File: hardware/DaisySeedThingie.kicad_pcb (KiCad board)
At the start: 2 copper layers, 236.2 x 124.5 mm, 66 parts, among them J1 LEDS, J10 AUDIO IN LR, J11 AUDIO IN L, J12 AUDIO IN R, J13 AUDIO OUT LR, J14 AUDIO OUT L, J15 AUDIO OUT R, J16 MIDI IN, J17 MIDI OUT, J18 MIDI IN, J19 MIDI OUT, J2 DC IN, J20 A, J21 B, J22 C, J23 D, J3 DAISY PINS, J4 COMPONENTS, J5 DAISY PINS, J6 Yamaichi PJS008-4100-0-VE, J7 MICRO SD, J8 AUDIO IN, J9 AUDIO OUT, SW1 ENCODER, SW2 A, SW3 C, SW4 B, SW5 D, U1 DAISY SEED, U2 H11L1, U3 128x64

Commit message: Restructure
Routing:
- net +3.3V: track 390.1 -> 0.00 mm, vias 1 -> 0
- net D0: track 352.6 -> 0.00 mm, vias 3 -> 0
- net D27: track 347.4 -> 0.00 mm, vias 2 -> 0
- net AUDIO_OUT_L: track 345.4 -> 0.00 mm, vias 4 -> 0
- net +VIN: track 337.7 -> 0.00 mm, vias 3 -> 0
- net D3: track 336.2 -> 0.00 mm, vias 3 -> 0
- net D9: track 331.9 -> 0.00 mm, vias 1 -> 0
- net AUDIO_IN_R: track 326.7 -> 0.00 mm, vias 3 -> 0
- net AUDIO_IN_L: track 322.2 -> 0.00 mm, vias 3 -> 0
- net AUDIO_OUT_R: track 310.4 -> 0.00 mm, vias 1 -> 0
- net D12: track 309.3 -> 0.00 mm, vias 3 -> 0
- net D10: track 303.1 -> 0.00 mm, vias 2 -> 0
- net D1: track 300.4 -> 0.00 mm, vias 3 -> 0
- net D11: track 295.0 -> 0.00 mm, vias 3 -> 0
- net D22: track 294.7 -> 0.00 mm, vias 4 -> 0
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
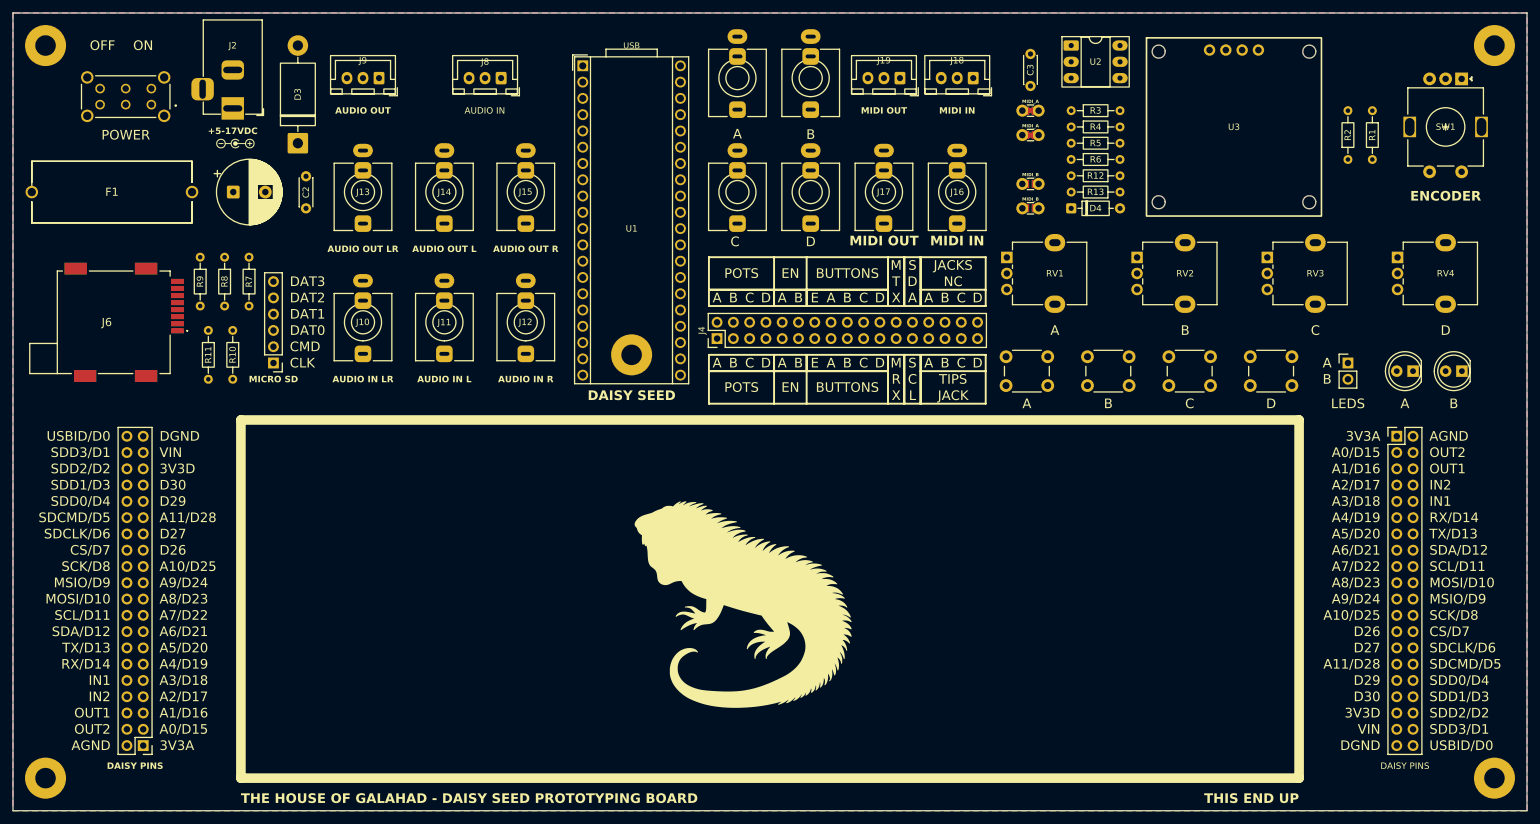
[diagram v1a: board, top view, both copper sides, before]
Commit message: Restore after bad merge
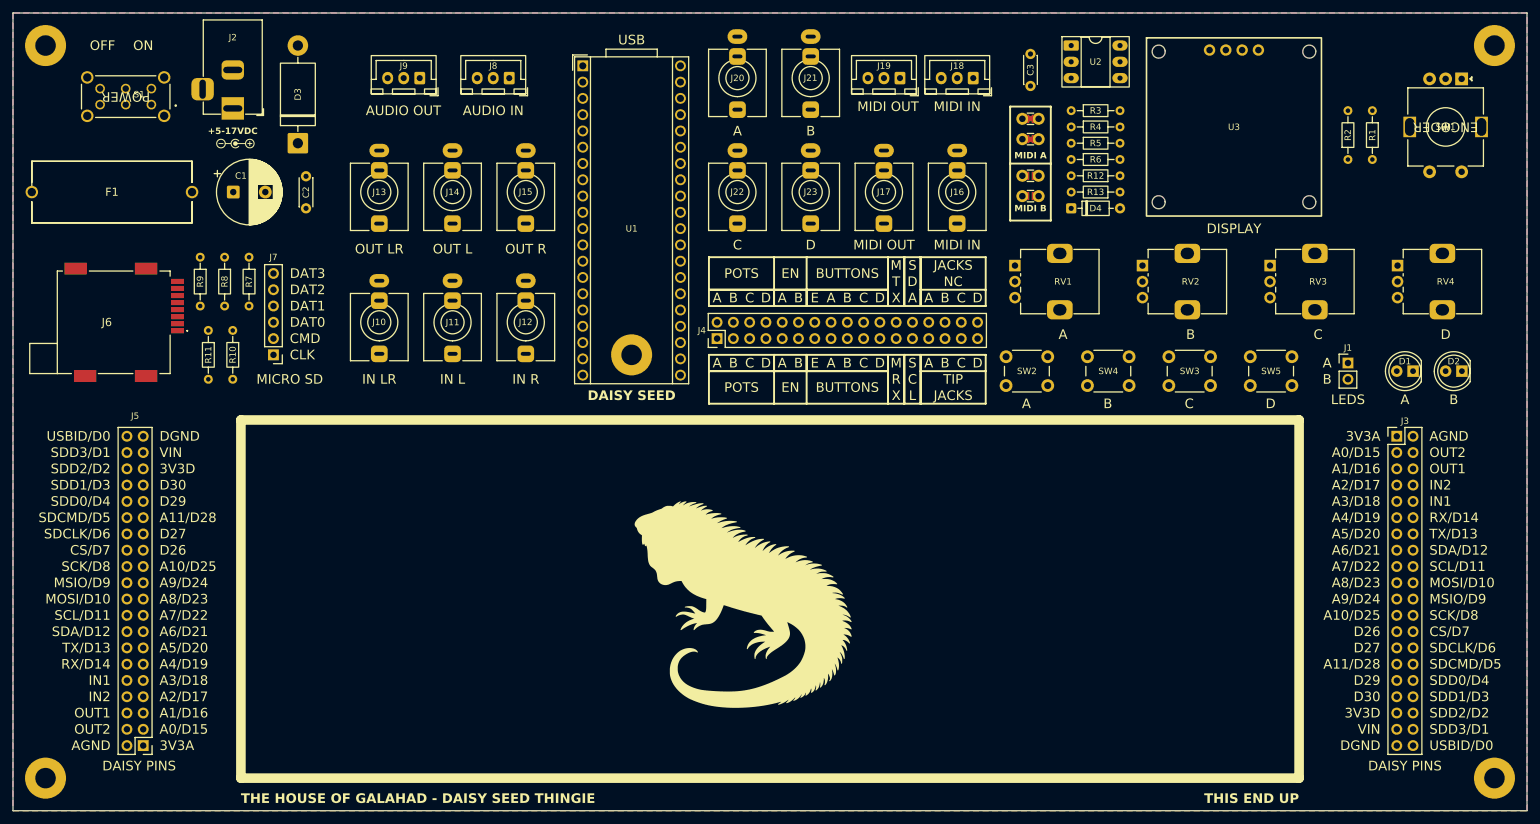
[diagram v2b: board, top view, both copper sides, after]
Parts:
- D1: value A -> RED
- D2: value B -> RED
- F1: value Fuse -> 5x20mm
- J1: value LEDS -> 01x02 PIN CONNECTOR
- J10: value AUDIO IN LR -> STEREO 3.5mm
- J11: value AUDIO IN L -> MONO 3.5mm
- J12: value AUDIO IN R -> MONO 3.5mm
- J13: value AUDIO OUT LR -> STEREO 3.5mm
- J14: value AUDIO OUT L -> MONO 3.5mm
- J15: value AUDIO OUT R -> MONO 3.5mm
- J16: value MIDI IN -> STEREO 3.5mm
- J17: value MIDI OUT -> STEREO 3.5mm
- J18: value MIDI IN -> JST 01x03
- J19: value MIDI OUT -> JST 01x03
- J2: value DC IN -> DC Barrel Jack
- J20: value A -> MONO 3.5mm
- J21: value B -> MONO 3.5mm
- J22: value C -> MONO 3.5mm
- J23: value D -> MONO 3.5mm
- J3, J5: value DAISY PINS -> 02x20 PIN CONNECTOR
- J4: value COMPONENTS -> 02x17 PIN CONNECTOR
- J7: value MICRO SD -> 01x06 PIN CONNECTOR
- J8: value AUDIO IN -> JST 01x03
- J9: value AUDIO OUT -> JST 01x03
- JP1, JP4: value MIDI_B -> JUMPER
- JP2, JP3: value MIDI_A -> JUMPER
- RV1, RV2, RV3, RV4: footprint Desval:Potentiometer_Alpha_RD901F-40-00D_Single_Vertical -> Desval:Potentiometer_Alps_RK09K_Single_Vertical
- S1: value POWER -> EG2219
- SW1: value ENCODER -> EN11C
- SW2: value A -> SW_PUSH_6mm
- SW3: value C -> SW_PUSH_6mm
- SW4: value B -> SW_PUSH_6mm
- SW5: value D -> SW_PUSH_6mm
- U3: value 128x64 -> SSD1306 0.96" OLED I2C
- moved J9 6.35 mm to (81.2, 53.3)
- moved J10 2.54 mm to (74.9, 91.4)
- moved J13 2.54 mm to (74.9, 71.1)
- moved JP4 1.91 mm to (176.5, 71.8), turned to 0 degrees
- moved RV1 1.80 mm to (181.6, 85.1), turned to 0 degrees
- moved RV2 1.53 mm to (201.5, 85.1), turned to 0 degrees
- moved RV3 1.34 mm to (221.4, 85.1), turned to 0 degrees
- moved J7 1.27 mm to (58.4, 96.5)
- moved RV4 1.27 mm to (241.3, 85.1), turned to 0 degrees
- moved J11 1.27 mm to (86.4, 91.4)
- moved J14 1.27 mm to (86.4, 71.1)
- moved J8 1.27 mm to (95.2, 53.3)
- moved JP1 1.27 mm to (176.5, 68.6), turned to 0 degrees
- moved JP2 1.27 mm to (176.5, 59.7), turned to 0 degrees
- moved JP3 0.64 mm to (176.5, 62.9), turned to 0 degrees
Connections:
- S1 pad S1: Net-(J2-Pad2) -> GND
- S1 pad S2: Net-(J2-Pad2) -> GND
- S1 pad S3: Net-(J2-Pad2) -> GND
- S1 pad S4: Net-(J2-Pad2) -> GND
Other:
- board text added: "${COMPANY} - ${TITLE}"
- board text added: "EMAIL: ${EMAIL} GITHUB: ${GITHUB}"
- board text added: "REV ${REVISION} - ${ISSUE_DATE}"
- board text added: "TIP"
- board text removed: "JACK"
- board text removed: "REV B - 2026-04-05 paul.f.burdette@gmail.com"
- board text removed: "THE HOUSE OF GALAHAD - DAISY SEED PROTOTYPING BOARD"
- board text removed: "TIPS"

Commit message: Initial Revision B
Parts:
- removed H5: MountingHole_Pad, MountingHole:MountingHole_3.2mm_M3_Pad
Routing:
- net GND: track 0.00 -> 883.1 mm, vias 0 -> 3
- net +3.3V: track 0.00 -> 384.5 mm, vias 0 -> 3
- net D2: track 0.00 -> 339.8 mm, vias 0 -> 2
- net D5: track 0.00 -> 339.3 mm, vias 0 -> 2
- net D3: track 0.00 -> 337.1 mm, vias 0 -> 2
- net +VIN: track 0.00 -> 335.0 mm, vias 0 -> 3
- net AUDIO_OUT_R: track 0.00 -> 334.6 mm, vias 0 -> 2
- net AUDIO_IN_R: track 0.00 -> 330.9 mm, vias 0 -> 3
- net D9: track 0.00 -> 327.6 mm, vias 0 -> 1
- net AUDIO_OUT_L: track 0.00 -> 324.8 mm, vias 0 -> 2
- net AUDIO_IN_L: track 0.00 -> 322.7 mm, vias 0 -> 3
- net D6: track 0.00 -> 320.8 mm, vias 0 -> 2
- net D25: track 0.00 -> 311.1 mm, vias 0 -> 3
- net D7: track 0.00 -> 310.3 mm, vias 0 -> 3
- net D1: track 0.00 -> 308.5 mm, vias 0 -> 2
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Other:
- outline, holes or cut-outs redrawn
